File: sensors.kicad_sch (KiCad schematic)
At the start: 23 parts, among them J5 JST SH, J6 JST SH, J7 JST SH, J8 JST SH, U11 BMI088

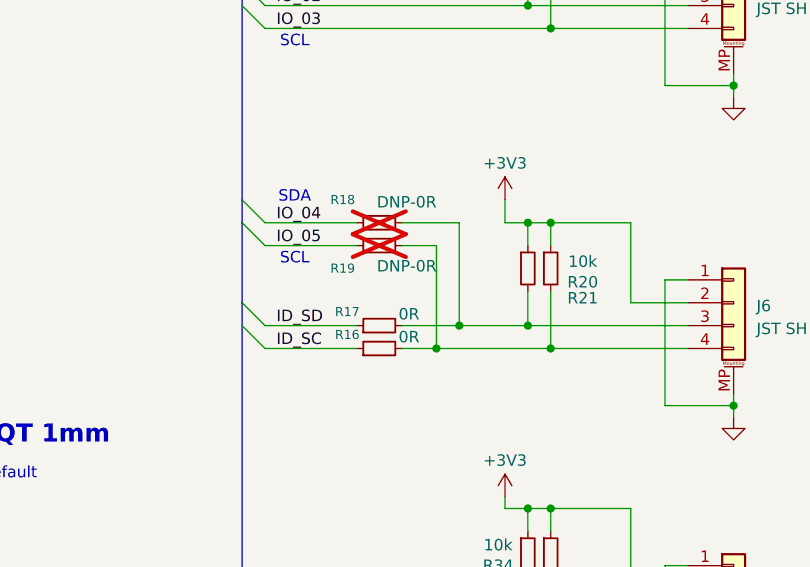
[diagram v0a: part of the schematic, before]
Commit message: [fix] Default I2C 0R
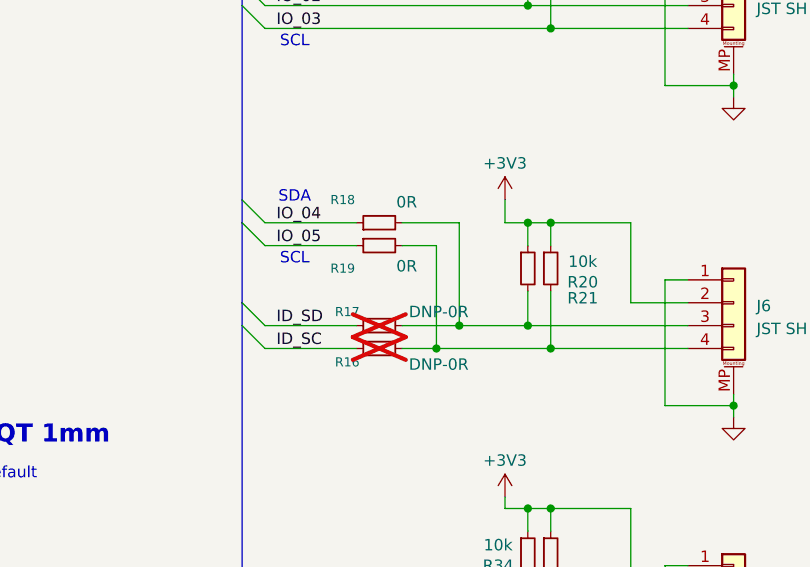
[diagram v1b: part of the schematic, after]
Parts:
- R16, R17: value 0R -> DNP-0R; LCSC Part C17168 -> (none); now not fitted
- R18, R19: value DNP-0R -> 0R; now fitted
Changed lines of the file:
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@@
 		(in_bom yes)
 		(on_board yes)
-		(dnp yes)
+		(dnp no)
 		(property "Reference" "R19"
 			(at 88.646 101.6 90)
@@
 			)
 		)
-		(property "Value" "DNP-0R"
+		(property "Value" "0R"
 			(at 95.758 101.346 90)
 			(effects
@@
 		(in_bom yes)
 		(on_board yes)
-		(dnp yes)
+		(dnp no)
 		(property "Reference" "R18"
 			(at 88.646 93.98 90)
@@
 			)
 		)
-		(property "Value" "DNP-0R"
+		(property "Value" "0R"
 			(at 95.758 94.234 90)
 			(effects
@@
 		(in_bom yes)
 		(on_board yes)
-		(dnp no)
+		(dnp yes)
 		(property "Reference" "R16"
-			(at 89.154 108.966 90)
+			(at 89.154 112.014 90)
 			(effects
 				(font
@@
 			)
 		)
-		(property "Value" "0R"
-			(at 96.012 109.22 90)
+		(property "Value" "DNP-0R"
+			(at 99.314 112.268 90)
 			(effects
 				(font
@@
 			)
 		)
-		(property "LCSC Part" "C17168"
+		(property "LCSC Part" ""
 			(at 92.71 110.49 90)
 			(effects
@@
 		(in_bom yes)
 		(on_board yes)
-		(dnp no)
+		(dnp yes)
 		(property "Reference" "R17"
 			(at 89.154 106.426 90)
@@
 			)
 		)
-		(property "Value" "0R"
-			(at 96.012 106.68 90)
+		(property "Value" "DNP-0R"
+			(at 99.314 106.426 90)
 			(effects
 				(font
@@
 			)
 		)
-		(property "LCSC Part" "C17168"
+		(property "LCSC Part" ""
 			(at 92.71 107.95 90)
 			(effects

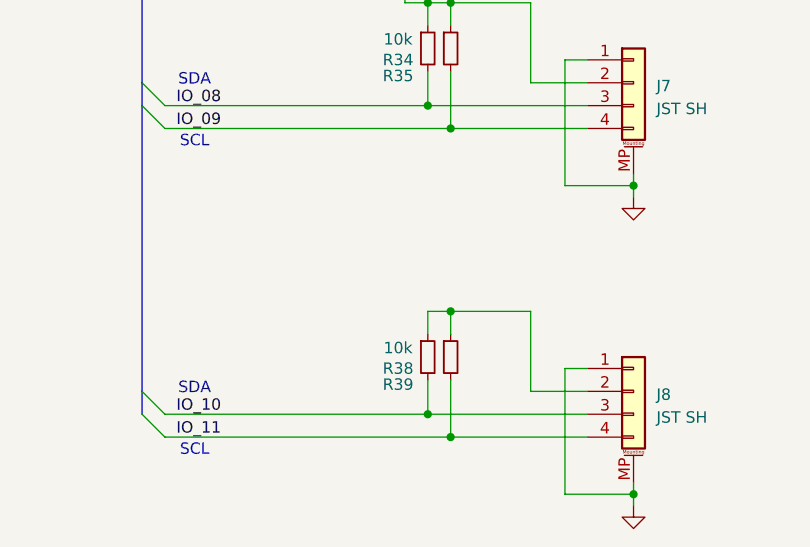
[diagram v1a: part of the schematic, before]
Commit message: [update] Release C1 (for Grabette), now qtty 20 @JLCPCB
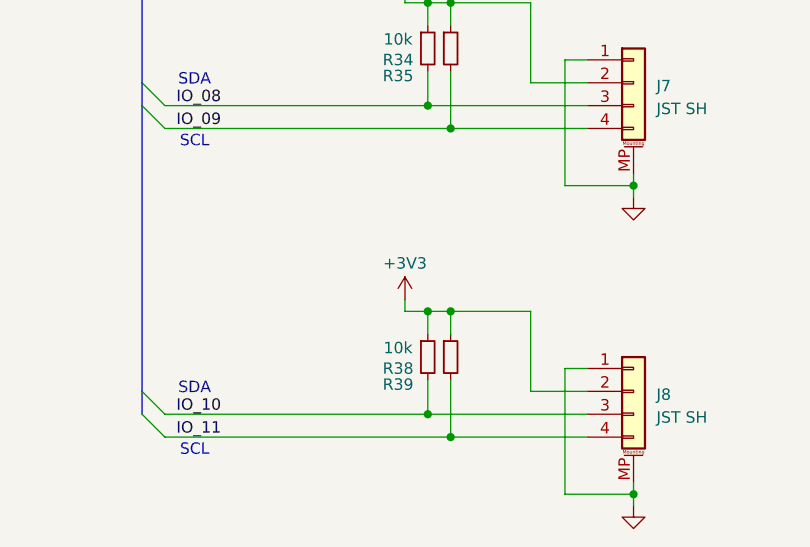
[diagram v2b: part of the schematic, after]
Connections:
- net +3V3: now also J8.2 (Pin_2), R38.1, R39.1
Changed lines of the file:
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@@
 	)
 	(junction
+		(at 109.22 162.56)
+		(diameter 0)
+		(color 0 0 0 0)
+	)
+	(junction
 		(at 111.76 110.49)
 		(diameter 0)
@@
 	(wire
 		(pts
+			(xy 106.68 162.56) (xy 109.22 162.56)
+		)
+		(stroke
+			(width 0)
+			(type default)
+		)
+	)
+	(wire
+		(pts
 			(xy 132.08 181.61) (xy 132.08 182.88)
 		)
@@
 	(wire
 		(pts
+			(xy 106.68 161.29) (xy 106.68 162.56)
+		)
+		(stroke
+			(width 0)
+			(type default)
+		)
+	)
+	(wire
+		(pts
 			(xy 127 134.62) (xy 124.46 134.62)
 		)
@@
 					(unit 1)
 				)
+			)
+		)
+	)
+	(symbol
+		(lib_id "power:+3V3")
+		(at 106.68 161.29 0)
+		(unit 1)
+		(exclude_from_sim no)
+		(in_bom yes)
+		(on_board yes)
+		(dnp no)
+		(property "Reference" "#PWR0104"
+			(at 106.68 165.1 0)
+			(effects
+				(font
+					(size 1.27 1.27)
+				)
+				(hide yes)
+			)
+		)
+		(property "Value" "+3V3"
+			(at 106.68 157.226 0)
+			(effects
+				(font
+					(size 1.27 1.27)
+				)
+			)
+		)
+		(property "Footprint" ""
+			(at 106.68 161.29 0)
+			(effects
+				(font
+					(size 1.27 1.27)
+				)
+				(hide yes)
+			)
+		)
+		(property "Datasheet" ""
+			(at 106.68 161.29 0)
+			(effects
+				(font
+					(size 1.27 1.27)
+				)
+				(hide yes)
+			)
+		)
+		(property "Description" "Power symbol creates a global label with name \"+3V3\""
+			(at 106.68 161.29 0)
+			(effects
+				(font
+					(size 1.27 1.27)
+				)
+				(hide yes)
+			)
+		)
+		(pin "1"
+		)
+		(instances
+			(project "elec_RPI_Robot_HAT"
+				(path "/bc05f5da-608c-4912-90e4-36b13d989976/d25b6afa-8f8a-4256-aaa0-d06d8816c749/7c72b1ef-1385-4d18-a22c-ca8fe94f1469"
+					(reference "#PWR0104")
+					(unit 1)
+				)

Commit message: [update] JLC-ready, time for Claude review
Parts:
- removed U11: BMI088, Package_LGA:Bosch_LGA-16_4.5x3mm_P0.5mm_LayoutBorder7x1y_ClockwisePinNumbering, symbol Sensor_Motion:BMI088
- added G1: qwiic_Logo, Library_Pollen:Logo_qwiic_5mm, symbol Library_Pollen:Logo qwiic
- added R30: 0R, Resistor_SMD:R_0402_1005Metric, symbol Device:R_Small
- added TP5: TestPoint, TestPoint:TestPoint_Pad_D1.0mm, symbol Connector:TestPoint
- added U12: LSM6DSV16XTR, Package_LGA:LGA-14_3x2.5mm_P0.5mm_LayoutBorder3x4y, symbol Sensor_Motion:LSM6DSM
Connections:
- net +3V3: now also U12.12 (CS); no longer R14.1
- net GND: now also R14.1, R30.1, U12.6 (GND), U12.7 (GND)
- net IO_02: now also U12.14 (SDA)
- net IO_03: now also U12.13 (SCL)
- net at R25.2: now also U12.4 (INT1)
- net at R15.2: now also U12.3 (SCX)
- net at C23.1, C24.2, R9.1: now also U12.5 (VDDIO), U12.8 (VDD)
- net at R14.2: now also U12.2 (SDX)
- new net: R30.2, U12.1 (SDO/SA0)
- new net: TP5.1, U12.9 (INT2)
- no-connect marks 5 -> 2
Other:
- note added: "I2C Addr: 0x6A"
- note removed: "I2C add.: - acc.: 0x19 - gyr.: 0x68"
- moved on the sheet: C23, C24, R14, R15, R25, R9
